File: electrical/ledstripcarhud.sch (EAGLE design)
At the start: 27 parts, among them IC1 DC-DC Step Down 5.2V, SW1 SWITCH-SPST-2RA, U1 TEENSY 3.2, U2 MCP2562, X1 OBD-II, X2 LED-STRIP

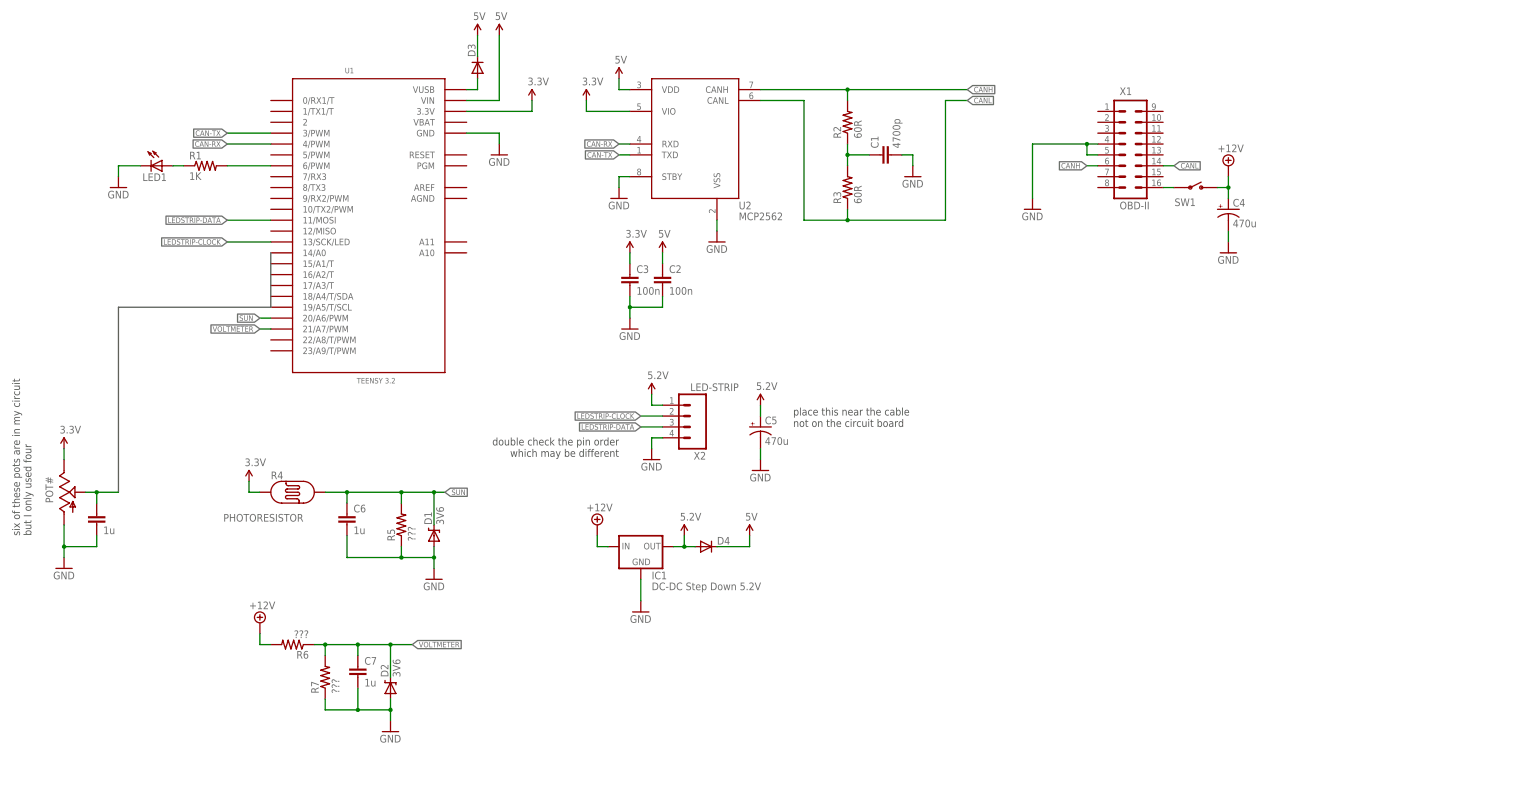
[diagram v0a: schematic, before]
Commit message: added level shifters to schematic
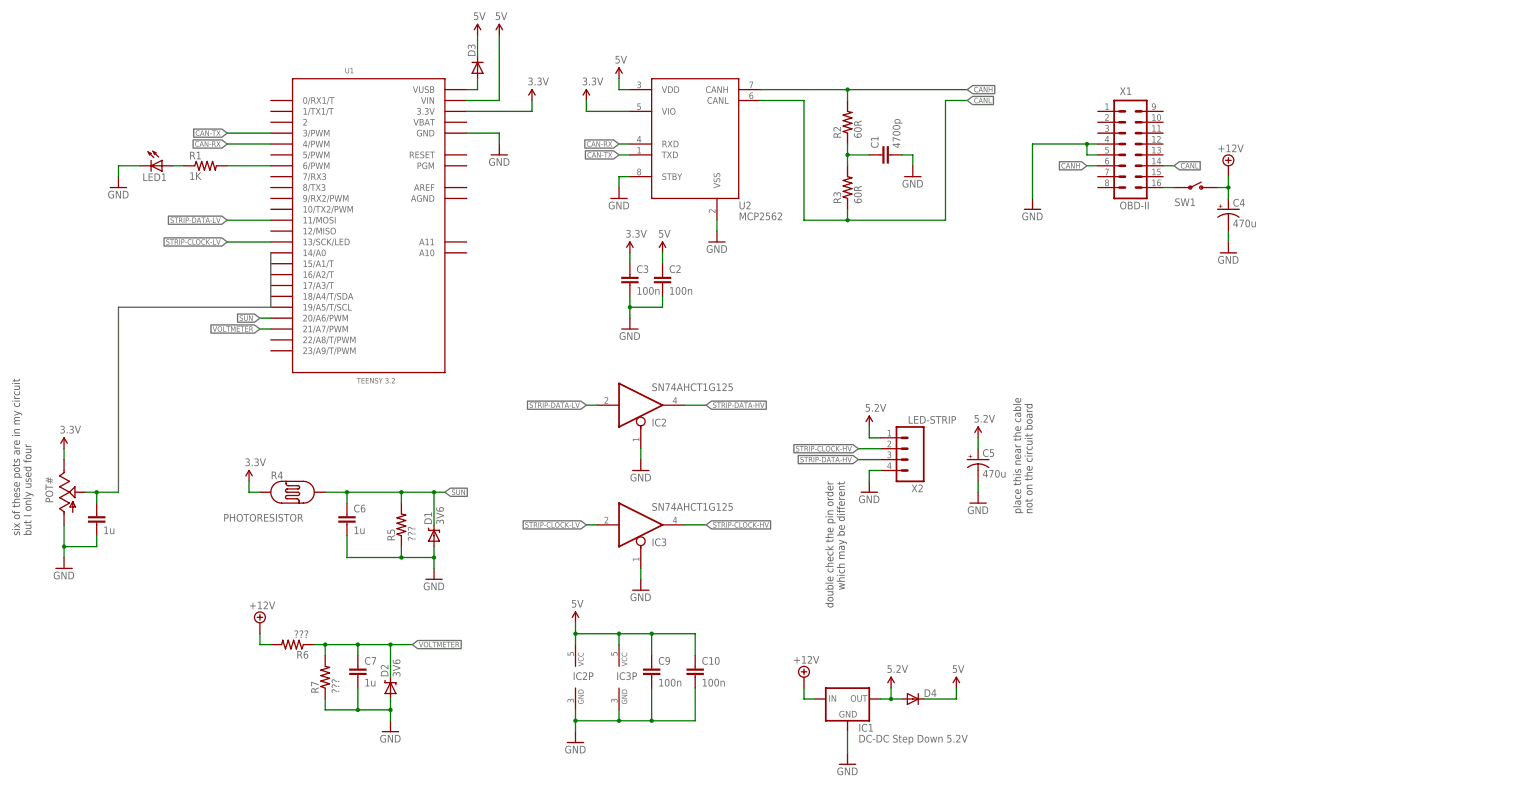
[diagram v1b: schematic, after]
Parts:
- added C10, C9: 100n, ledstripcarhud:CAP0603-CAP
- added IC2, IC3: SN74AHCT1G125, ledstripcarhud:74AHC1G125DBV
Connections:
- removed net LEDSTRIP-CLOCK: U1.13/SCK/LED, X2.2
- removed net LEDSTRIP-DATA: U1.11/MOSI, X2.3
- new net STRIP-CLOCK-HV: IC3A.O, X2.2
- new net STRIP-CLOCK-LV: IC3A.I, U1.13/SCK/LED
- new net STRIP-DATA-HV: IC2A.O, X2.3
- new net STRIP-DATA-LV: IC2A.I, U1.11/MOSI
- net 5V: now also C10.1, C9.1, IC2P.VCC, IC3P.VCC
- net GND: now also C10.2, C9.2, IC2A.OE, IC2P.GND, IC3A.OE, IC3P.GND
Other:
- moved on the sheet: C5, D4, IC1, X2

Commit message: added GPL text to everything
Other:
- note added: "This file is part of LedStripCarHud LedStripCarHud is free software: you can redistribute it and/or modify it under the terms of the GNU General Public License as published by the Free Software Foundation, either version 3 of the License, or (at your option) any later version. LedStripCarHud is distributed in the hope that it will be useful, but WITHOUT ANY WARRANTY; without even the implied warr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"
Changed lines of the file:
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@@
 <text x="-10.16" y="-22.86" size="1.778" layer="97" rot="R90">six of these pots are in my circuit
 but I only used four</text>
+<text x="228.6" y="-66.04" size="1.778" layer="94">This file is part of LedStripCarHud
+LedStripCarHud is free software: you can redistribute it and/or modify
+it under the terms of the GNU General Public License as published by
+the Free Software Foundation, either version 3 of the License, or
+(at your option) any later version.
+LedStripCarHud is distributed in the hope that it will be useful,
+but WITHOUT ANY WARRANTY; without even the implied warranty of
+MERCHANTABILITY or FITNESS FOR A PARTICULAR PURPOSE.  See the
+GNU General Public License for more details.
+You should have received a copy of the GNU General Public License
+along with LedStripCarHud.  If not, see &lt;http://www.gnu.org/licenses/&gt;.</text>
 </plain>
 <instances>
